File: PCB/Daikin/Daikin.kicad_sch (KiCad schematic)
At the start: 24 parts, among them J1 1x5, J2 Prog, Q3 PMF250XNEX, U1 ESP32-PICO-MINI-02, U2 LMR16006YDDCR, U3 QR

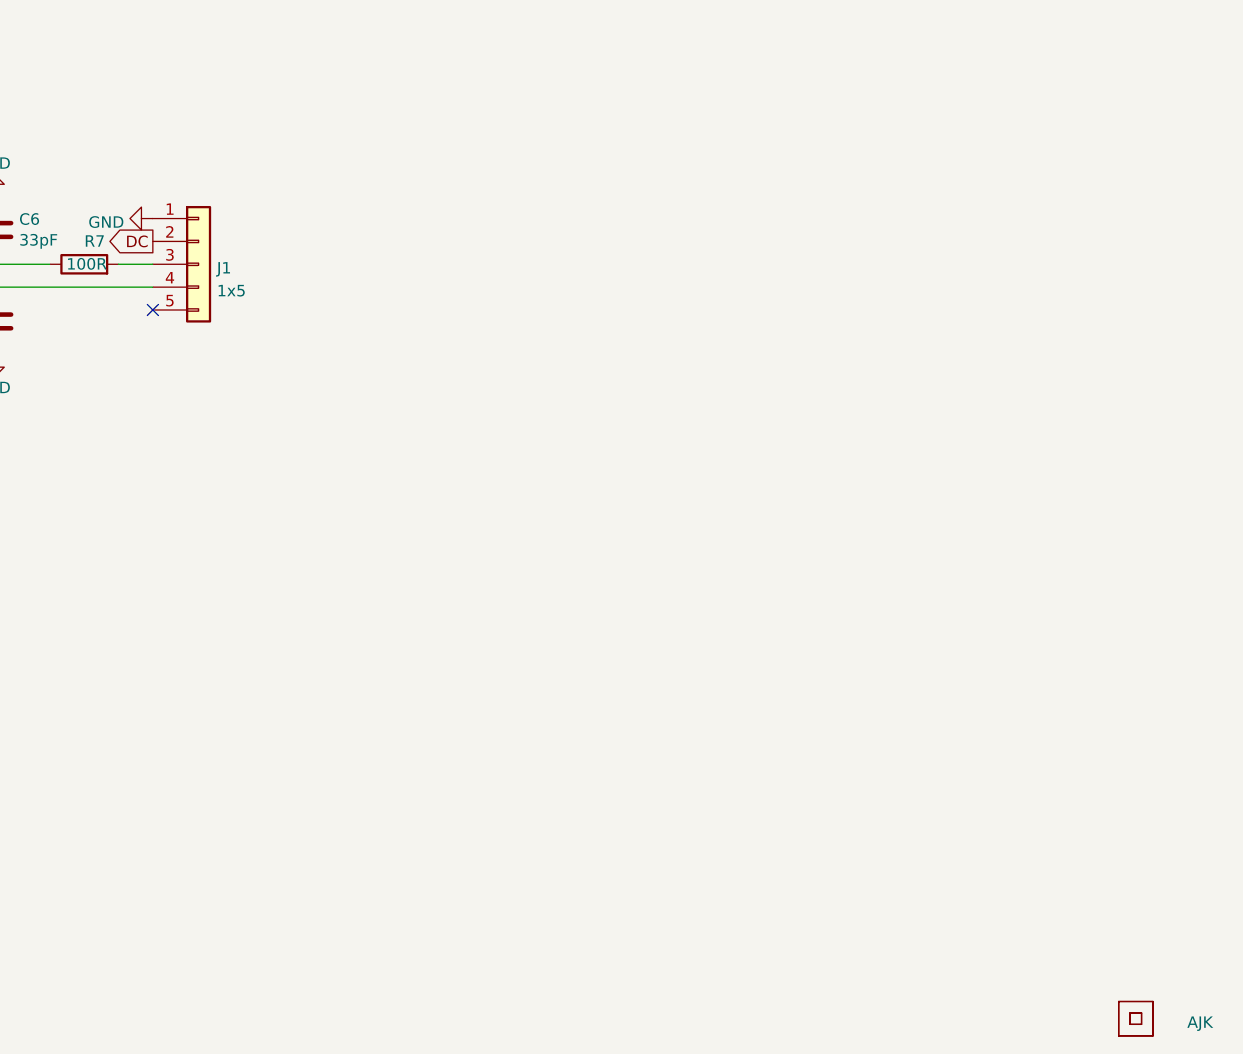
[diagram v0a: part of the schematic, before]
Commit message: New connector - matching what is on a Daikin
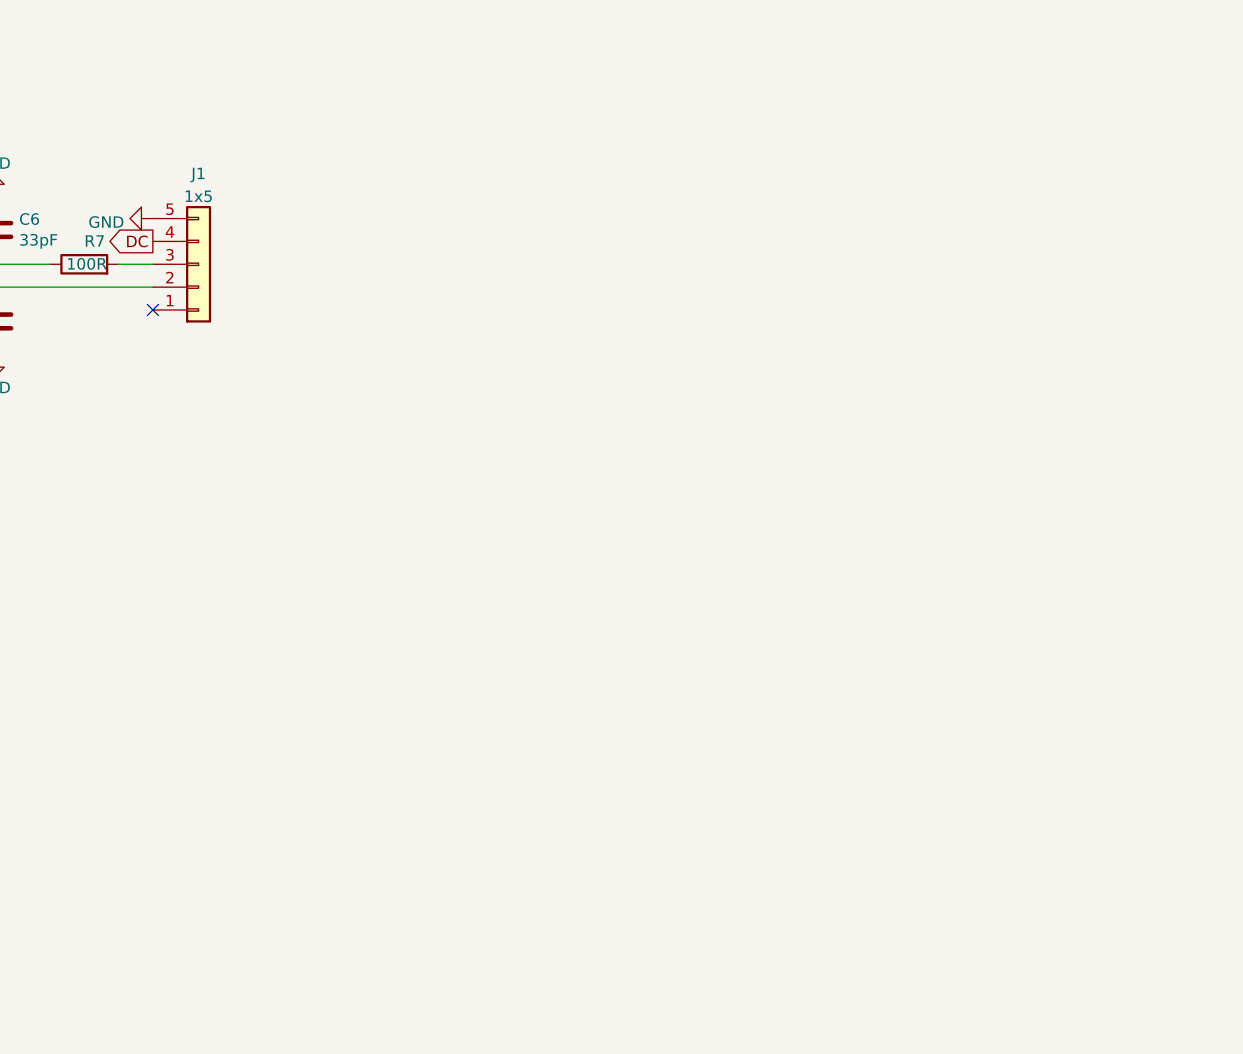
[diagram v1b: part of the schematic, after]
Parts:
- removed Logo1: AJK, RevK:AJK, symbol RevK:AJK
- removed U3: QR, RevK:QR-DAIKIN, symbol RevK:QR
- J1: footprint RevK:PinHeader_1x05_P2.54mm_Right -> Connector_JST:JST_EH_S5B-EH_1x05_P2.50mm_Horizontal; JLCPCB Position Offset (none) -> 5,0; LCSC Part # C225491 -> C225427
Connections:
- net DC: now also J1.4 (Pin_4); no longer J1.2 (Pin_2)
- net GND: now also J1.5 (Pin_5); no longer J1.1 (Pin_1)
- net at C7.2, Q3.1 (G): now also J1.2 (Pin_2); no longer J1.4 (Pin_4)
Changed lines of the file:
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@@
     (pin "2")
   )
-  (symbol (lib_id "Connector_Generic:Conn_01x05") (at 166.37 88.9 0) (unit 1)
-    (in_bom yes) (on_board yes) (fields_autoplaced)
-    (property "Reference" "J1" (id 0) (at 168.402 89.3353 0)
-      (effects (font (size 1.27 1.27)) (justify left))
-    )
-    (property "Value" "1x5" (id 1) (at 168.402 91.8722 0)
-      (effects (font (size 1.27 1.27)) (justify left))
-    )
-    (property "Footprint" "RevK:PinHeader_1x05_P2.54mm_Right" (id 2) (at 166.37 88.9 0)
+  (symbol (lib_id "Connector_Generic:Conn_01x05") (at 166.37 88.9 0) (mirror x) (unit 1)
+    (in_bom yes) (on_board yes) (fields_autoplaced)
+    (property "Reference" "J1" (id 0) (at 166.37 78.8502 0))
+    (property "Value" "1x5" (id 1) (at 166.37 81.3871 0))
+    (property "Footprint" "Connector_JST:JST_EH_S5B-EH_1x05_P2.50mm_Horizontal" (id 2) (at 166.37 88.9 0)
       (effects (font (size 1.27 1.27)) hide)
     )
@@
       (effects (font (size 1.27 1.27)) hide)
     )
-    (property "LCSC Part #" "C225491" (id 4) (at 166.37 88.9 0)
+    (property "LCSC Part #" "C225427" (id 4) (at 166.37 88.9 0)
+      (effects (font (size 1.27 1.27)) hide)
+    )
+    (property "JLCPCB Position Offset" "5,0" (id 5) (at 166.37 88.9 0)
       (effects (font (size 1.27 1.27)) hide)
     )
@@
     (pin "1")
   )
-  (symbol (lib_id "RevK:QR") (at 270.51 172.72 0) (unit 1)
-    (in_bom no) (on_board yes) (fields_autoplaced)
-    (property "Reference" "U3" (id 0) (at 270.51 175.895 0)
-      (effects (font (size 1.27 1.27)) hide)
-    )
-    (property "Value" "QR" (id 1) (at 270.51 175.895 0)
-      (effects (font (size 1.27 1.27)) hide)
-    )
-    (property "Footprint" "RevK:QR-DAIKIN" (id 2) (at 269.875 173.355 0)
-      (effects (font (size 1.27 1.27)) hide)
-    )
-    (property "Datasheet" "" (id 3) (at 269.875 173.355 0)
-      (effects (font (size 1.27 1.27)) hide)
-    )
-    (property "Note" "Non part, PCB printed" (id 4) (at 270.51 172.72 0)
-      (effects (font (size 1.27 1.27)) hide)
-    )
-  )
   (symbol (lib_id "Device:R") (at 132.08 42.545 90) (unit 1)
     (in_bom yes) (on_board yes)
@@
     (pin "5")
   )
-  (symbol (lib_id "RevK:AJK") (at 275.59 172.72 0) (unit 1)
-    (in_bom no) (on_board yes) (fields_autoplaced)
-    (property "Reference" "Logo1" (id 0) (at 275.59 170.18 0)
-      (effects (font (size 1.27 1.27)) hide)
-    )
-    (property "Value" "AJK" (id 1) (at 276.225 173.1538 0)
-      (effects (font (size 1.27 1.27)) (justify left))
-    )
-    (property "Footprint" "RevK:AJK" (id 2) (at 275.59 175.26 0)
-      (effects (font (size 1.27 1.27)) hide)
-    )
-    (property "Datasheet" "" (id 3) (at 275.59 175.26 0)
-      (effects (font (size 1.27 1.27)) hide)
-    )
-    (property "Note" "Non part, PCB printed" (id 4) (at 275.59 172.72 0)
-      (effects (font (size 1.27 1.27)) hide)
-    )
-  )
   (sheet_instances
     (path "/" (page "1"))
@@
     )
     (path "/af073fa6-a783-40f2-9751-692984a62ffc"
-      (reference "J1") (unit 1) (value "1x5") (footprint "RevK:PinHeader_1x05_P2.54mm_Right")
+      (reference "J1") (unit 1) (value "1x5") (footprint "Connector_JST:JST_EH_S5B-EH_1x05_P2.50mm_Horizontal")
     )
     (path "/ee567585-ddb7-4c4a-a692-94261f4c4bce"
@@
       (reference "L1") (unit 1) (value "6.8uH") (footprint "RevK:L_4x4_")
     )
-    (path "/f93331c2-c430-4421-8c6c-fa9ccbf3197e"
-      (reference "Logo1") (unit 1) (value "AJK") (footprint "RevK:AJK")
-    )
     (path "/ebcfdf36-110d-4f79-9de0-e4fcd76c1d6e"
       (reference "Q3") (unit 1) (value "PMF250XNEX") (footprint "RevK:SOT-323_SC-70")
@@
       (reference "U2") (unit 1) (value "LMR16006YDDCR") (footprint "RevK:SOT-23-Thin-6-Reg")
     )
-    (path "/dd024a75-cbfd-4a06-88fc-e180db89ebee"
-      (reference "U3") (unit 1) (value "QR") (footprint "RevK:QR-DAIKIN")
-    )
-  )
+  )

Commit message: Revised for production
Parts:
- C6: JLCPCB Rotation Offset (none) -> 90
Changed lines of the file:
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@@
+      (effects (font (size 1.27 1.27)) hide)
+    )
+    (property "JLCPCB Rotation Offset" "90" (id 7) (at 143.51 85.09 0)
       (effects (font (size 1.27 1.27)) hide)
     )

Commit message: Updated for correct JLC export
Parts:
- C6: JLCPCB Rotation Offset 90 -> (none)
- D1: JLCPCB Rotation Offset (none) -> 180
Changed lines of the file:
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@@
-      (effects (font (size 1.27 1.27)) hide)
-    )
-    (property "JLCPCB Rotation Offset" "90" (id 7) (at 143.51 85.09 0)
       (effects (font (size 1.27 1.27)) hide)
     )
@@
       (effects (font (size 1.27 1.27)) hide)
     )
+    (property "JLCPCB Rotation Offset" "180" (id 5) (at 66.04 116.84 0)
+      (effects (font (size 1.27 1.27)) hide)
+    )
